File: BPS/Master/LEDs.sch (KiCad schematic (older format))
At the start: 18 parts, among them J3 FrontFans, J4 BackFans

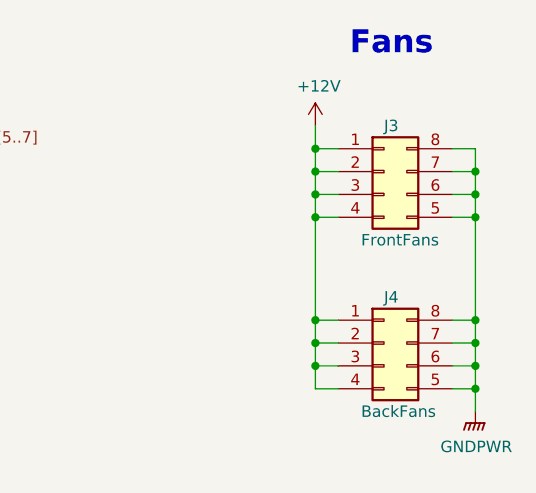
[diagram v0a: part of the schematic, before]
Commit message: Creates fan brd interface schematics and updates symbols/footprints related to the leader board
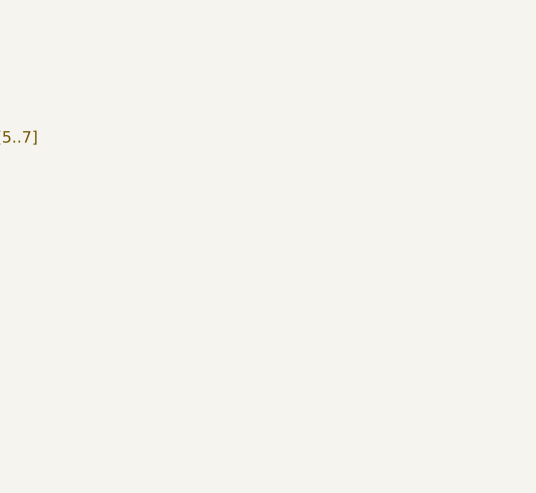
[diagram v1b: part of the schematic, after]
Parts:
- removed J3: FrontFans, UTSVT_Connectors:Molex_MicroFit3.0_2x4xP3.00mm_PolarizingPeg_Vertical, symbol Connector_Generic:Conn_02x04_Counter_Clockwise
- removed J4: BackFans, UTSVT_Connectors:Molex_MicroFit3.0_2x4xP3.00mm_PolarizingPeg_Vertical, symbol Connector_Generic:Conn_02x04_Counter_Clockwise
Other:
- note removed: "Fans"
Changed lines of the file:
@@
 $Descr A4 11693 8268
 encoding utf-8
-Sheet 4 9
+Sheet 4 10
 Title ""
 Date ""
@@
 Comment4 ""
 $EndDescr
-$Comp
-L Connector_Generic:Conn_02x04_Counter_Clockwise J3
-U 1 1 5C39DF85
-P 8350 2650
-F 0 "J3" H 8350 2850 50  0000 L CNN
-F 1 "FrontFans" H 8250 2350 50  0000 L CNN
-F 2 "UTSVT_Connectors:Molex_MicroFit3.0_2x4xP3.00mm_PolarizingPeg_Vertical" H 8350 2650 50  0001 C CNN
-F 3 "~" H 8350 2650 50  0001 C CNN
-	1    8350 2650
-	1    0    0    -1
-$EndComp
-Text Notes 8200 2150 0    100  ~ 20
-Fans
-$Comp
-L Connector_Generic:Conn_02x04_Counter_Clockwise J4
-U 1 1 5C39DFFD
-P 8350 3400
-F 0 "J4" H 8350 3600 50  0000 L CNN
-F 1 "BackFans" H 8250 3100 50  0000 L CNN
-F 2 "UTSVT_Connectors:Molex_MicroFit3.0_2x4xP3.00mm_PolarizingPeg_Vertical" H 8350 3400 50  0001 C CNN
-F 3 "~" H 8350 3400 50  0001 C CNN
-	1    8350 3400
-	1    0    0    -1
-$EndComp
-$Comp
-L power:+12V #PWR028
-U 1 1 5C39E1C8
-P 8050 2450
-F 0 "#PWR028" H 8050 2300 50  0001 C CNN
-F 1 "+12V" H 8065 2623 50  0000 C CNN
-F 2 "" H 8050 2450 50  0001 C CNN
-F 3 "" H 8050 2450 50  0001 C CNN
-	1    8050 2450
-	1    0    0    -1
-$EndComp
-Wire Wire Line
-	8050 2450 8050 2550
-Wire Wire Line
-	8050 2650 8150 2650
 Text HLabel 2100 2500 0    50   Input ~ 0
 PC[0..5]
@@
 $EndComp
 $Comp
-L power:GND #PWR029
+L power:GND #PWR030
 U 1 1 5C3C06CA
 P 2850 3700
-F 0 "#PWR029" H 2850 3450 50  0001 C CNN
+F 0 "#PWR030" H 2850 3450 50  0001 C CNN
 F 1 "GND" H 2855 3527 50  0000 C CNN
 F 2 "" H 2850 3700 50  0001 C CNN
@@
 Text HLabel 6500 2500 2    50   Input ~ 0
 PA[5..7]
-Wire Wire Line
-	8150 2550 8050 2550
-Connection ~ 8050 2550
-Wire Wire Line
-	8050 2550 8050 2650
-Wire Wire Line
-	8150 2750 8050 2750
-Wire Wire Line
-	8050 2750 8050 2650
-Connection ~ 8050 2650
-Wire Wire Line
-	8150 2850 8050 2850
-Wire Wire Line
-	8050 2850 8050 2750
-Connection ~ 8050 2750
-Wire Wire Line
-	8750 3700 8750 3600
-Wire Wire Line
-	8750 2850 8650 2850
-Wire Wire Line
-	8750 2850 8750 2750
-Wire Wire Line
-	8750 2550 8650 2550
-Connection ~ 8750 2850
-Wire Wire Line
-	8650 2750 8750 2750
-Connection ~ 8750 2750
-Wire Wire Line
-	8750 2750 8750 2650
-Wire Wire Line
-	8650 2650 8750 2650
-Connection ~ 8750 2650
-Wire Wire Line
-	8750 2650 8750 2550
-Wire Wire Line
-	8650 3600 8750 3600
-Connection ~ 8750 3600
-Wire Wire Line
-	8750 3600 8750 3500
-Wire Wire Line
-	8650 3500 8750 3500
-Connection ~ 8750 3500
-Wire Wire Line
-	8750 3500 8750 3400
-Wire Wire Line
-	8650 3400 8750 3400
-Connection ~ 8750 3400
-Wire Wire Line
-	8750 3400 8750 3300
-Wire Wire Line
-	8650 3300 8750 3300
-Connection ~ 8750 3300
-Wire Wire Line
-	8750 3300 8750 2850
-Wire Wire Line
-	8050 2850 8050 3300
-Wire Wire Line
-	8050 3300 8150 3300
-Connection ~ 8050 2850
-Wire Wire Line
-	8050 3300 8050 3400
-Wire Wire Line
-	8050 3400 8150 3400
-Connection ~ 8050 3300
-Wire Wire Line
-	8050 3400 8050 3500
-Wire Wire Line
-	8050 3500 8150 3500
-Connection ~ 8050 3400
-Wire Wire Line
-	8050 3500 8050 3600
-Wire Wire Line
-	8050 3600 8150 3600
-Connection ~ 8050 3500
-$Comp
-L power:GNDPWR #PWR030
-U 1 1 5C82C789
-P 8750 3700
-F 0 "#PWR030" H 8750 3500 50  0001 C CNN
-F 1 "GNDPWR" H 8754 3546 50  0000 C CNN
-F 2 "" H 8750 3650 50  0001 C CNN
-F 3 "" H 8750 3650 50  0001 C CNN
-	1    8750 3700
-	1    0    0    -1
-$EndComp
 $Comp
 L Device:LED_ALT D9
